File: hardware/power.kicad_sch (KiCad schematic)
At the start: 45 parts, among them J1 B2B-PH-K-S, J2 USB4110-GF-A, J3 PRPC001DAAN-RC, J4 PRPC001DAAN-RC, J5 PRPC001DAAN-RC, J6 PRPC001DAAN-RC, J7 PRPC001DAAN-RC, Q1 IRLML2246TRPBF, Q2 DMN2046U-7, Q3 DMN2046U-7, Q4 IRLML2246TRPBF, U1 USBLC6-2SC6, U2 S-8240ADQ-M6T1U, U3 MCP73811T-420I-OT, U4 TPS61023DRLR

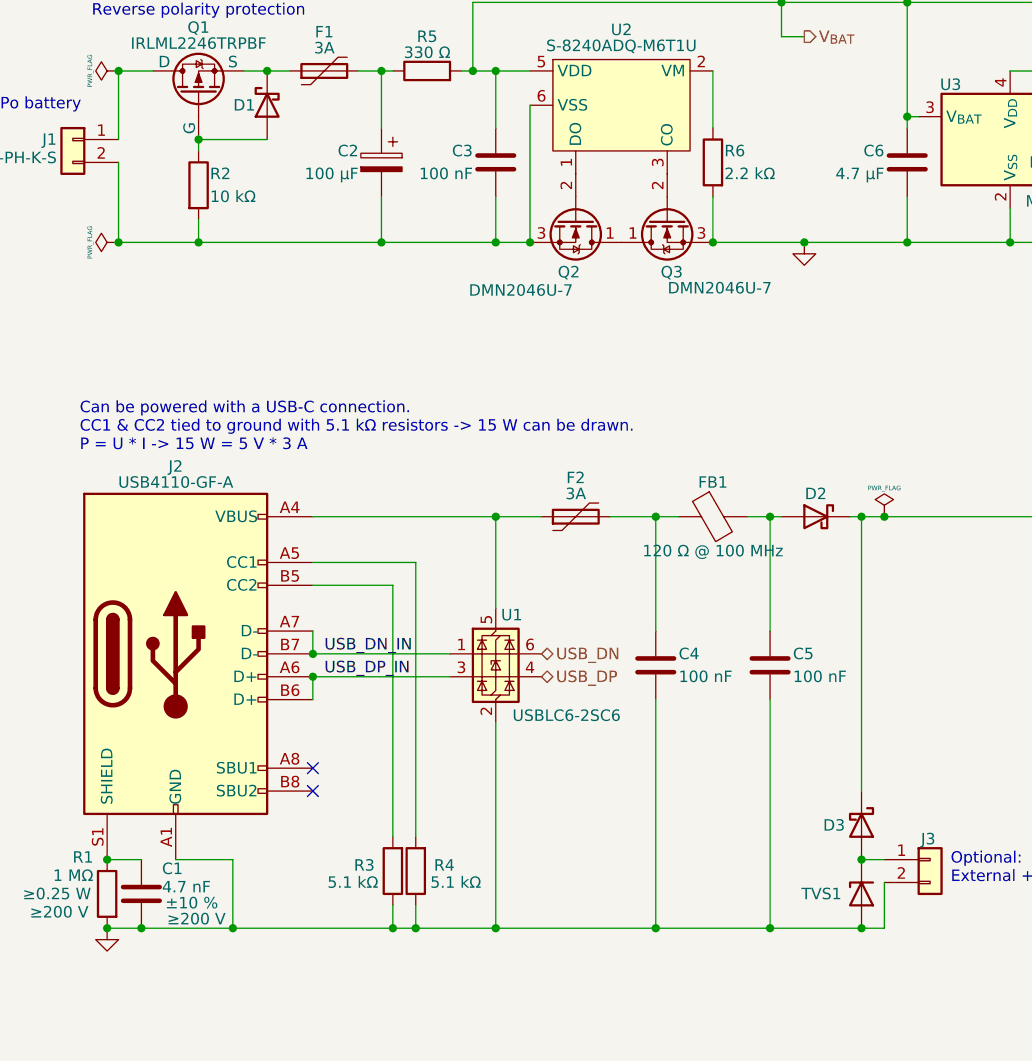
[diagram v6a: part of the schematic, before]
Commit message: HW: Replace 0402 with 0603 or bigger
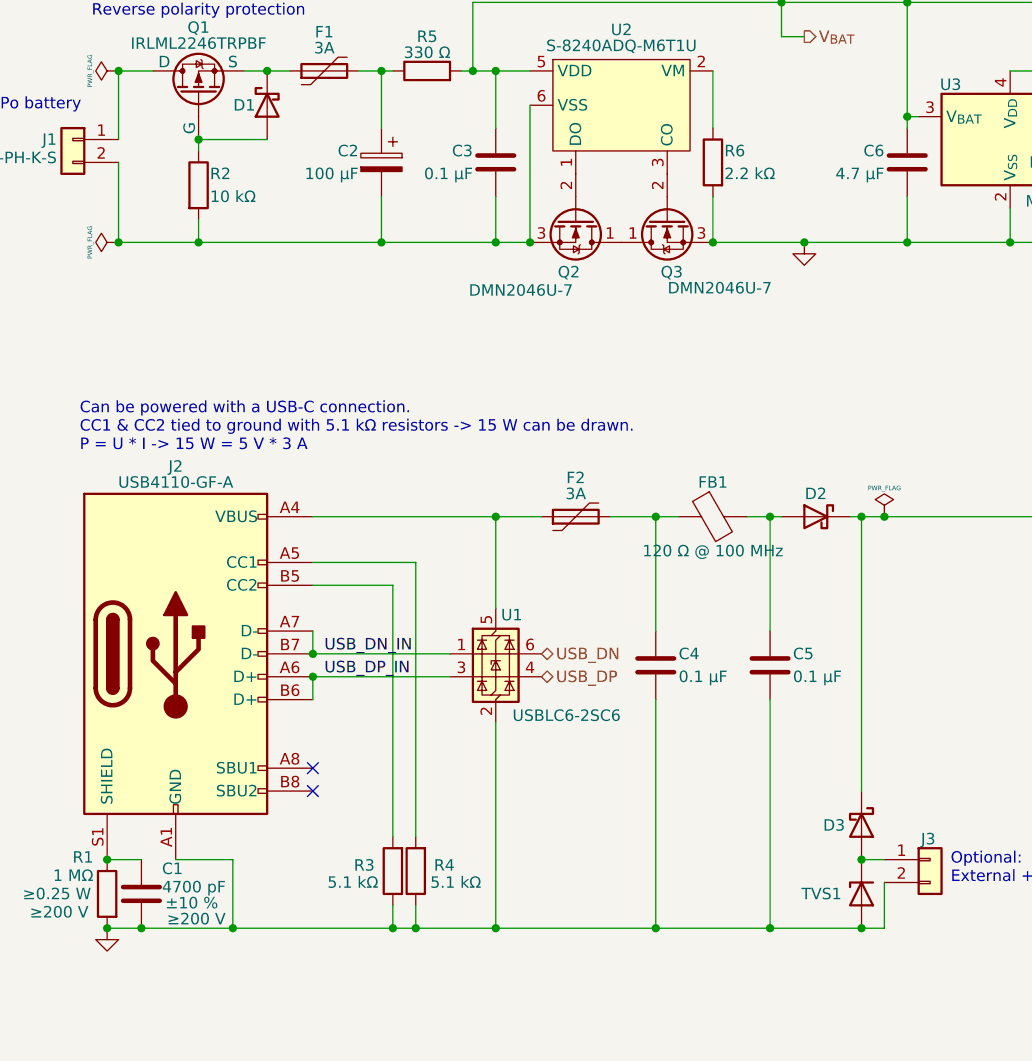
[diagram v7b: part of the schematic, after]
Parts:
- C1: value 4.7 nF -> 4700 pF; footprint Capacitor_SMD:C_0805_2012Metric_Pad1.18x1.45mm_HandSolder -> Capacitor_SMD:C_0603_1608Metric_Pad1.08x0.95mm_HandSolder
- C3, C4, C5: value 100 nF -> 0.1 µF; footprint Capacitor_SMD:C_0402_1005Metric_Pad0.74x0.62mm_HandSolder -> Capacitor_SMD:C_0603_1608Metric_Pad1.08x0.95mm_HandSolder; Digi-Key Part Number 732-7513-1-ND -> 732-7989-1-ND; Manufacturer Part Number 885012205018 -> 885012206071
- C6, C7, C8, C9: Digi-Key Part Number 1276-1044-1-ND -> 732-7902-1-ND; Manufacturer Samsung Electro-Mechanics -> Würth Elektronik; Manufacturer Part Number CL10A475KP8NNNC -> 885012106005
- R10: footprint Resistor_SMD:R_0402_1005Metric_Pad0.72x0.64mm_HandSolder -> Resistor_SMD:R_0603_1608Metric_Pad0.98x0.95mm_HandSolder; Digi-Key Part Number 732-560112110217CT-ND -> 732-560112116066CT-ND; Manufacturer Part Number 560112110217 -> 560112116066
- R2, R7: footprint Resistor_SMD:R_0402_1005Metric_Pad0.72x0.64mm_HandSolder -> Resistor_SMD:R_0603_1608Metric_Pad0.98x0.95mm_HandSolder; Digi-Key Part Number 732-560112110020CT-ND -> 732-560112116005CT-ND; Manufacturer Part Number 560112110020 -> 560112116005
- R5: footprint Resistor_SMD:R_0805_2012Metric_Pad1.20x1.40mm_HandSolder -> Resistor_SMD:R_0603_1608Metric_Pad0.98x0.95mm_HandSolder; Digi-Key Part Number 732-560112120017CT-ND -> 732-560112116020CT-ND; Manufacturer Part Number 560112120017 -> 560112116020
- R6, R8: footprint Resistor_SMD:R_0402_1005Metric_Pad0.72x0.64mm_HandSolder -> Resistor_SMD:R_0603_1608Metric_Pad0.98x0.95mm_HandSolder; Digi-Key Part Number 732-560112110087CT-ND -> 732-560112116098CT-ND; Manufacturer Part Number 560112110087 -> 560112116098
- TVS1: value PE1605M1Q_R1_00001 -> SMAJ6.0CA-13-F; footprint Diode_SMD:D_0402_1005Metric_Pad0.77x0.64mm_HandSolder -> Diode_SMD:D_SMA_Handsoldering; Digi-Key Part Number 3757-PE1605M1Q_R1_00001CT-ND -> SMAJ6.0CA-13-FDICT-ND; Manufacturer Panjit International Inc. -> Diodes Incorporated; Manufacturer Part Number PE1605M1Q_R1_00001 -> SMAJ6.0CA-13-F
- U2: footprint Package_TO_SOT_SMD:SOT-23-6 -> Package_TO_SOT_SMD:SOT-23-6_Handsoldering
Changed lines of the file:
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@@
 			)
 		)
-		(property "Footprint" "Resistor_SMD:R_0402_1005Metric_Pad0.72x0.64mm_HandSolder"
+		(property "Footprint" "Resistor_SMD:R_0603_1608Metric_Pad0.98x0.95mm_HandSolder"
 			(at 182.118 57.15 90)
 			(effects
@@
 			)
 		)
-		(property "Manufacturer Part Number" "560112110020"
+		(property "Manufacturer Part Number" "560112116005"
 			(at 180.34 57.15 0)
 			(effects
@@
 			)
 		)
-		(property "Digi-Key Part Number" "732-560112110020CT-ND"
+		(property "Digi-Key Part Number" "732-560112116005CT-ND"
 			(at 180.34 57.15 0)
 			(effects
@@
 			)
 		)
-		(property "Value" "100 nF"
+		(property "Value" "0.1 µF"
 			(at 77.47 60.96 0)
 			(effects
@@
 			)
 		)
-		(property "Footprint" "Capacitor_SMD:C_0402_1005Metric_Pad0.74x0.62mm_HandSolder"
+		(property "Footprint" "Capacitor_SMD:C_0603_1608Metric_Pad1.08x0.95mm_HandSolder"
 			(at 79.0448 63.5 0)
 			(effects
@@
 			)
 		)
-		(property "Manufacturer Part Number" "885012205018"
+		(property "Manufacturer Part Number" "885012206071"
 			(at 80.01 59.69 0)
 			(effects
@@
 			)
 		)
-		(property "Digi-Key Part Number" "732-7513-1-ND"
+		(property "Digi-Key Part Number" "732-7989-1-ND"
 			(at 80.01 59.69 0)
 			(effects
@@
 			)
 		)
-		(property "Manufacturer" "Samsung Electro-Mechanics"
+		(property "Manufacturer" "Würth Elektronik"
 			(at 125.73 59.69 0)
 			(effects
@@
 			)
 		)
-		(property "Manufacturer Part Number" "CL10A475KP8NNNC"
+		(property "Manufacturer Part Number" "885012106005"
 			(at 125.73 59.69 0)
 			(effects
@@
 			)
 		)
-		(property "Digi-Key Part Number" "1276-1044-1-ND"
+		(property "Digi-Key Part Number" "732-7902-1-ND"
 			(at 125.73 59.69 0)
 			(effects
@@
 			)
 		)
-		(property "Manufacturer" "Samsung Electro-Mechanics"
+		(property "Manufacturer" "Würth Elektronik"
 			(at 151.13 57.15 0)
 			(effects
@@
 			)
 		)
-		(property "Manufacturer Part Number" "CL10A475KP8NNNC"
+		(property "Manufacturer Part Number" "885012106005"
 			(at 151.13 57.15 0)
 			(effects
@@
 			)
 		)
-		(property "Digi-Key Part Number" "1276-1044-1-ND"
+		(property "Digi-Key Part Number" "732-7902-1-ND"
 			(at 151.13 57.15 0)
 			(effects
@@
 			)
 		)
-		(property "Value" "4.7 nF"
+		(property "Value" "4700 pF"
 			(at 42.926 140.208 0)
 			(effects
@@
 			)
 		)
-		(property "Footprint" "Capacitor_SMD:C_0805_2012Metric_Pad1.18x1.45mm_HandSolder"
+		(property "Footprint" "Capacitor_SMD:C_0603_1608Metric_Pad1.08x0.95mm_HandSolder"
 			(at 41.6052 144.78 0)
 			(effects
@@
 			)
 		)
-		(property "Manufacturer" "Samsung Electro-Mechanics"
+		(property "Manufacturer" "Würth Elektronik"
 			(at 257.81 57.15 0)
 			(effects
@@
 			)
 		)
-		(property "Manufacturer Part Number" "CL10A475KP8NNNC"
+		(property "Manufacturer Part Number" "885012106005"
 			(at 257.81 57.15 0)
 			(effects
@@
 			)
 		)
-		(property "Digi-Key Part Number" "1276-1044-1-ND"
+		(property "Digi-Key Part Number" "732-7902-1-ND"
 			(at 257.81 57.15 0)
 			(effects
@@
 			)
 		)
-		(property "Footprint" "Resistor_SMD:R_0402_1005Metric_Pad0.72x0.64mm_HandSolder"
+		(property "Footprint" "Resistor_SMD:R_0603_1608Metric_Pad0.98x0.95mm_HandSolder"
 			(at 105.918 59.69 90)
 			(effects
@@
 			)
 		)
-		(property "Digi-Key Part Number" "732-560112110087CT-ND"
+		(property "Digi-Key Part Number" "732-560112116098CT-ND"
 			(at 104.14 59.69 0)
 			(effects
@@
 			)
 		)
-		(property "Manufacturer Part Number" "560112110087"
+		(property "Manufacturer Part Number" "560112116098"
 			(at 104.14 59.69 0)
 			(effects
@@
 			)
 		)
-		(property "Value" "100 nF"
+		(property "Value" "0.1 µF"
 			(at 113.03 116.84 0)
 			(effects
@@
 			)
 		)
-		(property "Footprint" "Capacitor_SMD:C_0402_1005Metric_Pad0.74x0.62mm_HandSolder"
+		(property "Footprint" "Capacitor_SMD:C_0603_1608Metric_Pad1.08x0.95mm_HandSolder"
 			(at 111.4552 119.38 0)
 			(effects
@@
 			)
 		)
-		(property "Manufacturer Part Number" "885012205018"
+		(property "Manufacturer Part Number" "885012206071"
 			(at 110.49 115.57 0)
 			(effects
@@
 			)
 		)
-		(property "Digi-Key Part Number" "732-7513-1-ND"
+		(property "Digi-Key Part Number" "732-7989-1-ND"
 			(at 110.49 115.57 0)
 			(effects
@@
 			)
 		)
-		(property "Footprint" "Resistor_SMD:R_0402_1005Metric_Pad0.72x0.64mm_HandSolder"
+		(property "Footprint" "Resistor_SMD:R_0603_1608Metric_Pad0.98x0.95mm_HandSolder"
 			(at 45.212 62.23 90)
 			(effects
@@
 			)
 		)
-		(property "Manufacturer Part Number" "560112110020"
+		(property "Manufacturer Part Number" "560112116005"
 			(at 46.99 62.23 0)
 			(effects
@@
 			)
 		)
-		(property "Digi-Key Part Number" "732-560112110020CT-ND"
+		(property "Digi-Key Part Number" "732-560112116005CT-ND"
 			(at 46.99 62.23 0)
 			(effects
@@
 			)
 		)
-		(property "Footprint" "Package_TO_SOT_SMD:SOT-23-6"
+		(property "Footprint" "Package_TO_SOT_SMD:SOT-23-6_Handsoldering"
 			(at 93.98 62.992 0)
 			(effects
@@
 			)
 		)
-		(property "Value" "100 nF"
+		(property "Value" "0.1 µF"
 			(at 100.33 116.84 0)
 			(effects
@@
 			)
 		)
-		(property "Footprint" "Capacitor_SMD:C_0402_1005Metric_Pad0.74x0.62mm_HandSolder"
+		(property "Footprint" "Capacitor_SMD:C_0603_1608Metric_Pad1.08x0.95mm_HandSolder"
 			(at 98.7552 119.38 0)
 			(effects
@@
 			)
 		)
-		(property "Manufacturer Part Number" "885012205018"
+		(property "Manufacturer Part Number" "885012206071"
 			(at 97.79 115.57 0)
 			(effects
@@
 			)
 		)
-		(property "Digi-Key Part Number" "732-7513-1-ND"
+		(property "Digi-Key Part Number" "732-7989-1-ND"
 			(at 97.79 115.57 0)
 			(effects
@@
 			)
 		)
-		(property "Footprint" "Resistor_SMD:R_0402_1005Metric_Pad0.72x0.64mm_HandSolder"
+		(property "Footprint" "Resistor_SMD:R_0603_1608Metric_Pad0.98x0.95mm_HandSolder"
 			(at 227.838 135.89 90)
 			(effects
@@
 			)
 		)
-		(property "Digi-Key Part Number" "732-560112110087CT-ND"
+		(property "Digi-Key Part Number" "732-560112116098CT-ND"
 			(at 226.06 135.89 0)
 			(effects
@@
 			)
 		)
-		(property "Manufacturer Part Number" "560112110087"
+		(property "Manufacturer Part Number" "560112116098"
 			(at 226.06 135.89 0)
 			(effects
@@
 			)
 		)
-		(property "Value" "PE1605M1Q_R1_00001"
+		(property "Value" "SMAJ6.0CA-13-F"
 			(at 110.49 142.24 90)
 			(effects
@@
 			)
 		)
-		(property "Footprint" "Diode_SMD:D_0402_1005Metric_Pad0.77x0.64mm_HandSolder"
+		(property "Footprint" "Diode_SMD:D_SMA_Handsoldering"
 			(at 120.65 140.97 0)
 			(effects
@@
 			)
 		)
-		(property "Digi-Key Part Number" "3757-PE1605M1Q_R1_00001CT-ND"
+		(property "Digi-Key Part Number" "SMAJ6.0CA-13-FDICT-ND"
 			(at 120.65 140.97 0)
 			(effects
@@
 			)
 		)
-		(property "Manufacturer" "Panjit International Inc."
+		(property "Manufacturer" "Diodes Incorporated"
 			(at 120.65 140.97 0)
 			(effects
@@
 			)
 		)
-		(property "Manufacturer Part Number" "PE1605M1Q_R1_00001"
+		(property "Manufacturer Part Number" "SMAJ6.0CA-13-F"
 			(at 120.65 140.97 0)
 			(effects
@@
 			)
 		)
-		(property "Footprint" "Resistor_SMD:R_0805_2012Metric_Pad1.20x1.40mm_HandSolder"
+		(property "Footprint" "Resistor_SMD:R_0603_1608Metric_Pad0.98x0.95mm_HandSolder"
 			(at 72.39 51.308 90)
 			(effects
@@
 			)
 		)
-		(property "Digi-Key Part Number" "732-560112120017CT-ND"
+		(property "Digi-Key Part Number" "732-560112116020CT-ND"
 			(at 72.39 49.53 90)
 			(effects
@@
 			)
 		)
-		(property "Manufacturer Part Number" "560112120017"
+		(property "Manufacturer Part Number" "560112116020"
 			(at 72.39 49.53 90)
 			(effects
@@
 			)
 		)
-		(property "Footprint" "Resistor_SMD:R_0402_1005Metric_Pad0.72x0.64mm_HandSolder"
+		(property "Footprint" "Resistor_SMD:R_0603_1608Metric_Pad0.98x0.95mm_HandSolder"
 			(at 245.872 60.96 90)
 			(effects
@@
 			)
 		)
-		(property "Digi-Key Part Number" "732-560112110217CT-ND"
+		(property "Digi-Key Part Number" "732-560112116066CT-ND"
 			(at 247.65 60.96 0)
 			(effects
@@
 			)
 		)
-		(property "Manufacturer Part Number" "560112110217"
+		(property "Manufacturer Part Number" "560112116066"
 			(at 247.65 60.96 0)
 			(effects
@@
 			)
 		)
-		(property "Manufacturer" "Samsung Electro-Mechanics"
+		(property "Manufacturer" "Würth Elektronik"
 			(at 220.98 57.15 0)
 			(effects
@@
 			)
 		)
-		(property "Manufacturer Part Number" "CL10A475KP8NNNC"
+		(property "Manufacturer Part Number" "885012106005"
 			(at 220.98 57.15 0)
 			(effects
@@
 			)
 		)
-		(property "Digi-Key Part Number" "1276-1044-1-ND"
+		(property "Digi-Key Part Number" "732-7902-1-ND"
 			(at 220.98 57.15 0)
 			(effects

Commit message: HW: Layout power section
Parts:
- removed U4: TPS61023DRLR, Package_TO_SOT_SMD:SOT-563, symbol TPS61023DRL:TPS61023DRLR
- added U4: TPS62A01PDDCR, Package_TO_SOT_SMD:SOT-23-6, symbol TPS62A0:TPS62A01PDDCR
- C6, C7, C8: Digi-Key Part Number 732-7902-1-ND -> 732-7623-1-ND; Manufacturer Part Number 885012106005 -> 885012107013
- C9: value 4.7 µF -> 22 µF; footprint Capacitor_SMD:C_0603_1608Metric_Pad1.08x0.95mm_HandSolder -> Capacitor_SMD:C_0805_2012Metric_Pad1.18x1.45mm_HandSolder; Digi-Key Part Number 732-7902-1-ND -> 732-7616-1-ND; Manufacturer Part Number 885012106005 -> 885012107005
- L1: value 2.7 µH -> 1 µH; footprint Inductor_SMD:L_Bourns-SRU8028_8.0x8.0mm -> Inductor_SMD:L_1008_2520Metric_Pad1.43x2.20mm_HandSolder; Digi-Key Part Number 118-SRU8028A-2R5YCT-ND -> 490-13053-1-ND; Manufacturer Bourns Inc. -> Murata Electronics; Manufacturer Part Number SRU8028A-2R5Y -> DFE252012F-1R0M=P2
- R10: value 220 kΩ -> 100 kΩ; Digi-Key Part Number 732-560112116066CT-ND -> 732-560112116004CT-ND; Manufacturer Part Number 560112116066 -> 560112116004
- R9: value 1 MΩ -> 453 kΩ; footprint Resistor_SMD:R_1206_3216Metric_Pad1.30x1.75mm_HandSolder -> Resistor_SMD:R_0603_1608Metric_Pad0.98x0.95mm_HandSolder; Digi-Key Part Number 732-560112132011CT-ND -> 311-453KHRCT-ND; Manufacturer Würth Elektronik -> YAGEO; Manufacturer Part Number 560112132011 -> RC0603FR-07453KL
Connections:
- net GND: now also U4.2 (GND)
- net VOUT_{3V3}: now also L1.2
- net at R10.1, R9.2: now also U4.6 (FB)
- net at C8.1, D4.1 (K), D5.1 (K): now also U4.1 (EN), U4.4 (V_{IN}); no longer L1.1
- new net: L1.1, U4.3 (SW)
- no-connect marks 2 -> 3
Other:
- note added: "Buck-Boost regulator with soft start TPS62A01PDDCR datasheet: 8.2.2.1 Setting the output voltage: R1 = R2 * ((V_{OUT} / V_{FB}) - 1) Where V_{FB} = 0.6 V, R1 is the higher resistor and R2 is the lower resistor. R1 = 100 kΩ * ((3.3 V / 0.6 V) - 1) = 450 kΩ"
- note removed: "Buck-Boost regulator with soft start TPS61023 datasheet: 8.2.2.1 Setting the output voltage: R1 = ((V_{OUT} / V_{REF}) - 1) * R2 R2 = (R1 * V_{REF}) / (3.3 V - V_{REF}) Where V_{REF} ~= 0.6 V R2 = (1M Ω * 0.6 V) / (3.3 V - 0.6 V) = 222222 Ω"
- moved on the sheet: C8, C9, L1
